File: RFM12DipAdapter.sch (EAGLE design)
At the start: 5 parts

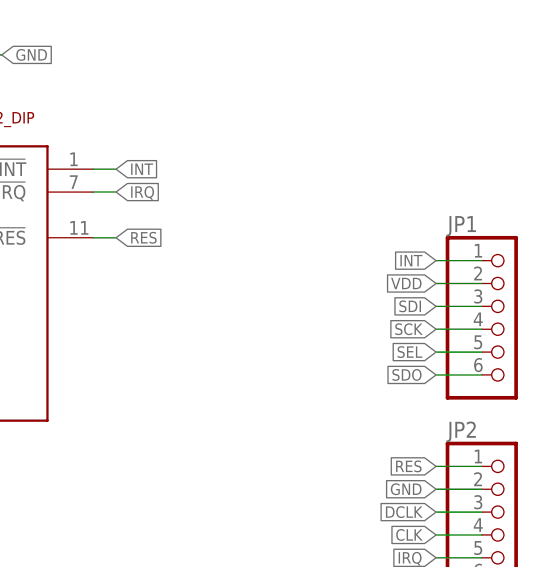
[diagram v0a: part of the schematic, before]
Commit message: Forgot VCC line
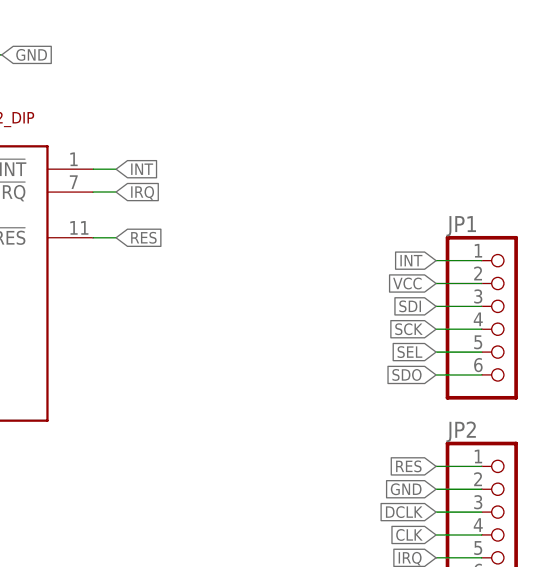
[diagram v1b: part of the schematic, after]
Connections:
- removed net VDD: JP1.2
- net VCC: now also JP1.2
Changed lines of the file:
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@@
 <label x="99.06" y="109.22" size="1.27" layer="95" rot="R90" xref="yes"/>
+</segment>
+<segment>
+<pinref part="JP1" gate="A" pin="2"/>
+<wire x1="165.1" y1="81.28" x2="160.02" y2="81.28" width="0.1524" layer="91"/>
+<label x="160.02" y="81.28" size="1.27" layer="95" rot="R180" xref="yes"/>
 </segment>
 </net>
@@
 </segment>
 </net>
-<net name="VDD" class="0">
-<segment>
-<pinref part="JP1" gate="A" pin="2"/>
-<wire x1="165.1" y1="81.28" x2="160.02" y2="81.28" width="0.1524" layer="91"/>
-<label x="160.02" y="81.28" size="1.27" layer="95" rot="R180" xref="yes"/>
-</segment>
-</net>
